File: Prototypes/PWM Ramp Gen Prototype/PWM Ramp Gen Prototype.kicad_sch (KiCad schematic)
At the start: 10 parts, among them J1 Conn_01x03, J2 Conn_01x03, J3 Conn_01x10

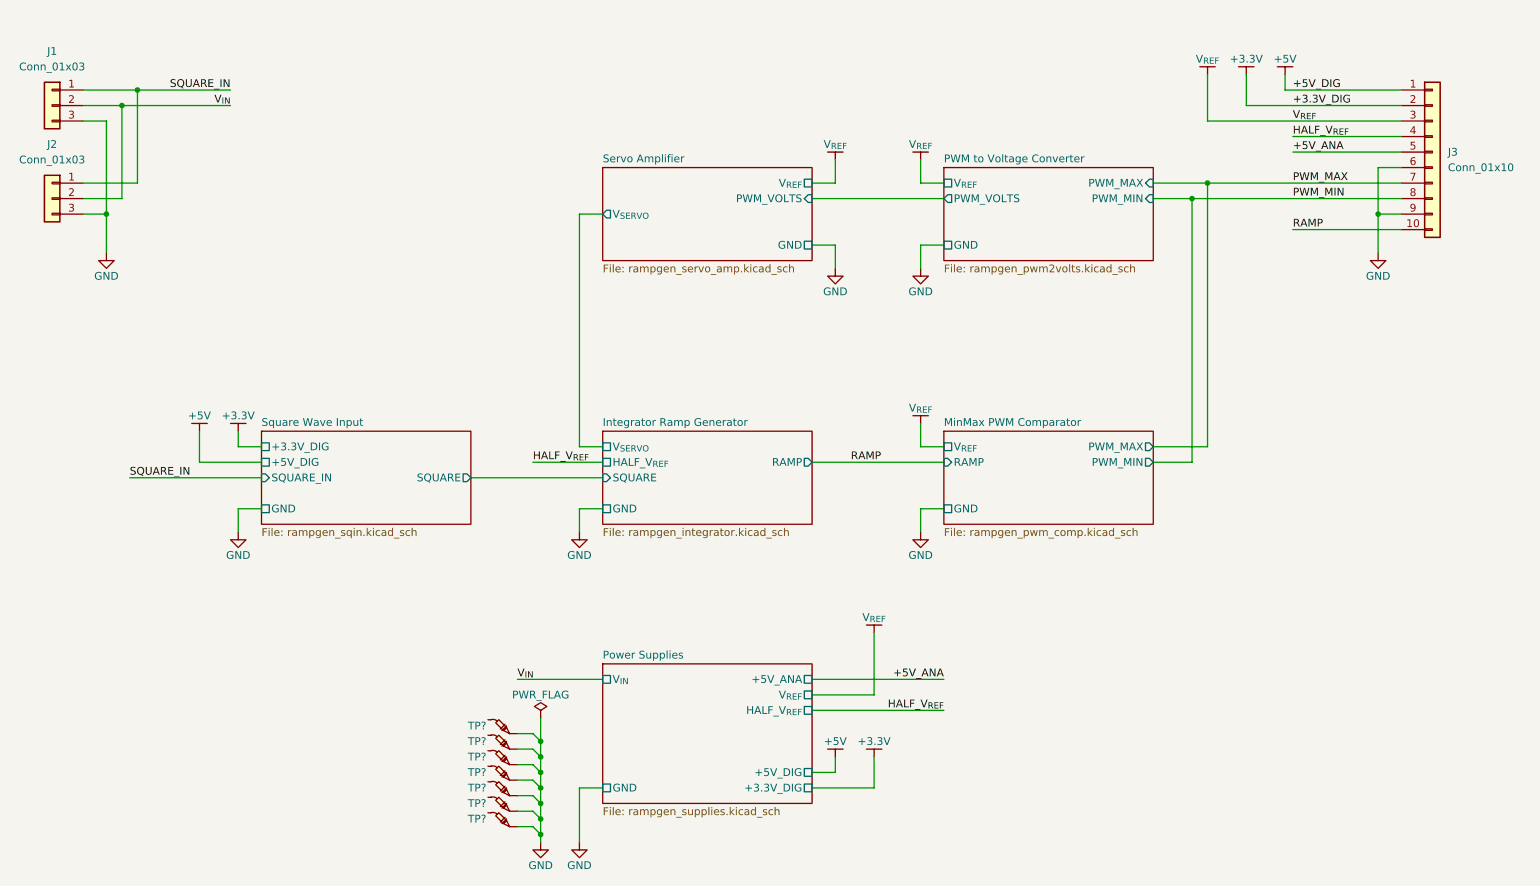
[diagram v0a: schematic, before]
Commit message: Comparator and Op-amp tweaks for BOM consolidation; final layout
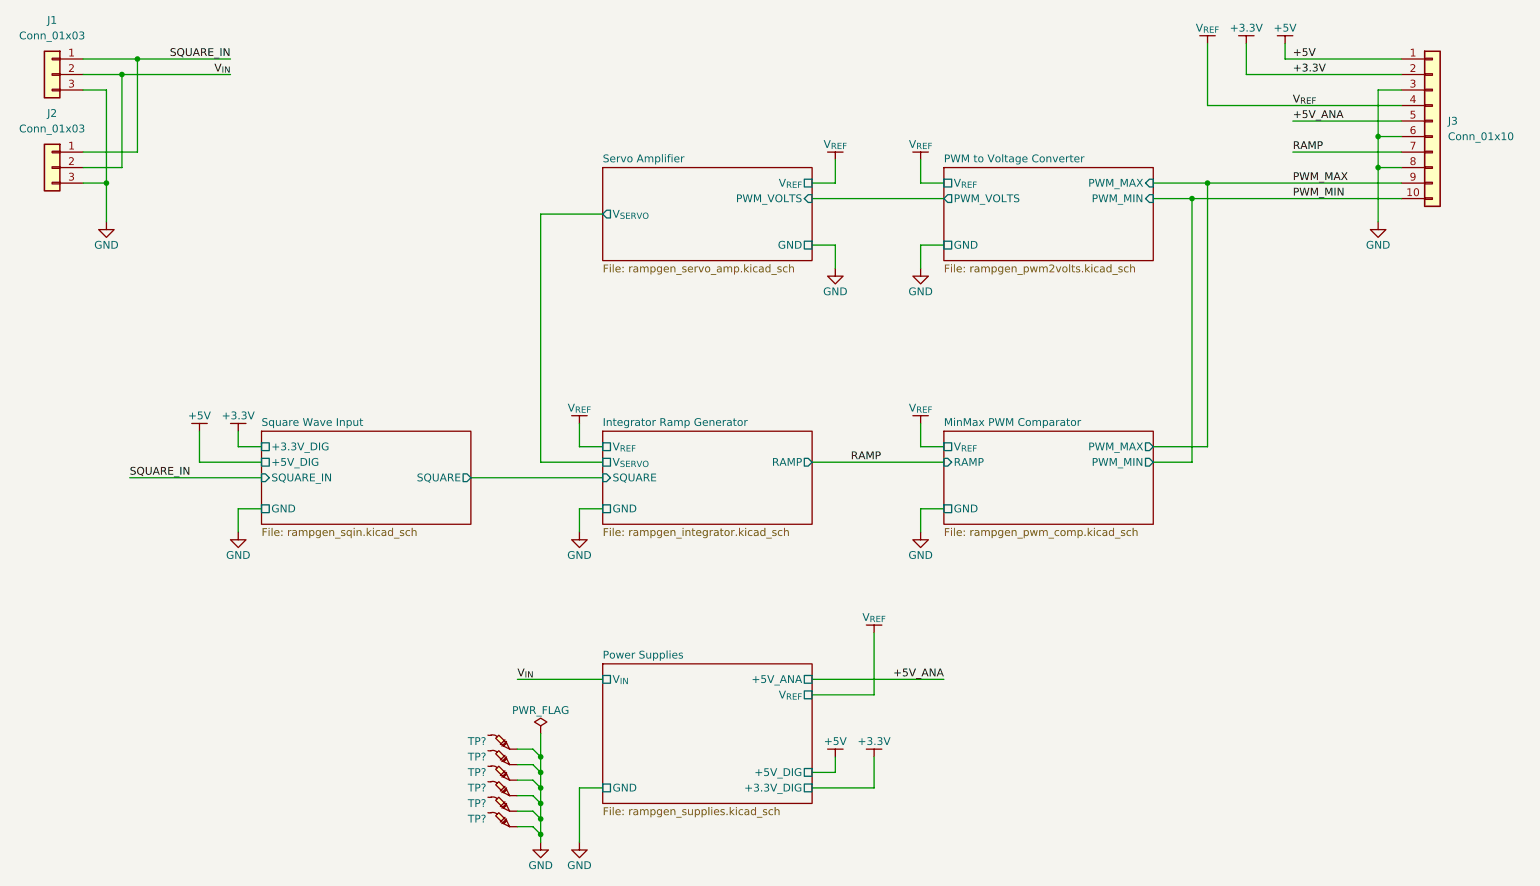
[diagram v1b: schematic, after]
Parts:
- removed TP?: -, TestPoint:TestPoint_Pad_D2.0mm, symbol Custom-LogicIC:TestPoint
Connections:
- net HALF_V_{REF} is gone; now on net V_{REF}: J3.4 (Pin_4)
- net GND: now also J3.3 (Pin_3), J3.8 (Pin_8); no longer J3.9 (Pin_9)
- net PWM_MAX: now also J3.9 (Pin_9); no longer J3.7 (Pin_7)
- net PWM_MIN: now also J3.10 (Pin_10); no longer J3.8 (Pin_8)
- net RAMP: now also J3.7 (Pin_7); no longer J3.10 (Pin_10)
- net V_{REF}: no longer J3.3 (Pin_3)
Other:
- sheet Integrator Ramp Generator ports: added V_{REF}; removed HALF_V_{REF}
- sheet Power Supplies ports: added none; removed HALF_V_{REF}
- moved on the sheet: J1, J2, J3, TP?
